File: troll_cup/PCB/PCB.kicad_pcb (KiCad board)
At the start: 2 copper layers, 45 x 45 mm, 13 parts, among them SW1 LEFT_BTN, SW2 RT_BTN, U1 ATtiny85-20P, U2 DFR0299

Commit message: New footprint
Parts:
- C1: footprint Capacitor_SMD:C_0603_1608Metric_Pad1.08x0.95mm_HandSolder -> Capacitor_THT:C_Disc_D5.0mm_W2.5mm_P2.50mm; moved to B.Cu
- R1: footprint Resistor_SMD:R_0805_2012Metric_Pad1.20x1.40mm_HandSolder -> Resistor_THT:R_Axial_DIN0204_L3.6mm_D1.6mm_P5.08mm_Horizontal; moved to B.Cu
- R2: footprint Resistor_SMD:R_0805_2012Metric_Pad1.20x1.40mm_HandSolder -> Resistor_THT:R_Axial_DIN0207_L6.3mm_D2.5mm_P7.62mm_Horizontal; moved to B.Cu
- SW1, SW2: footprint Library:Keypad -> Library:Keypad 2
- moved SW1 10.0 mm to (50.0, 68.5), turned to -90 degrees
- moved R2 5.90 mm to (77.0, 77.8)
- moved R1 4.65 mm to (62.0, 76.5)
- moved C1 2.61 mm to (58.0, 62.2)
- moved U1 1.41 mm to (65.2, 70.2)
- moved BAT1 1.00 mm to (66.0, 82.5)
- moved SPK1 1.00 mm to (77.0, 82.5)
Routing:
- net /VDD: track 130.8 -> 0.00 mm
- net /GND: track 47.7 -> 0.00 mm
- net Net-(U1-PB1): track 30.9 -> 0.00 mm
- net Net-(U1-XTAL2/PB4): track 28.1 -> 0.00 mm
- net Net-(SPK1-Pin_1): track 24.7 -> 0.00 mm
- net Net-(U2-TX): track 19.4 -> 0.00 mm
- net Net-(SPK1-Pin_2): track 18.9 -> 0.00 mm
- net Net-(U1-XTAL1/PB3): track 17.9 -> 0.00 mm
- net Net-(U1-AREF/PB0): track 7.55 -> 0.00 mm
- net Net-(U1-~{RESET}/PB5): track 3.27 -> 0.00 mm

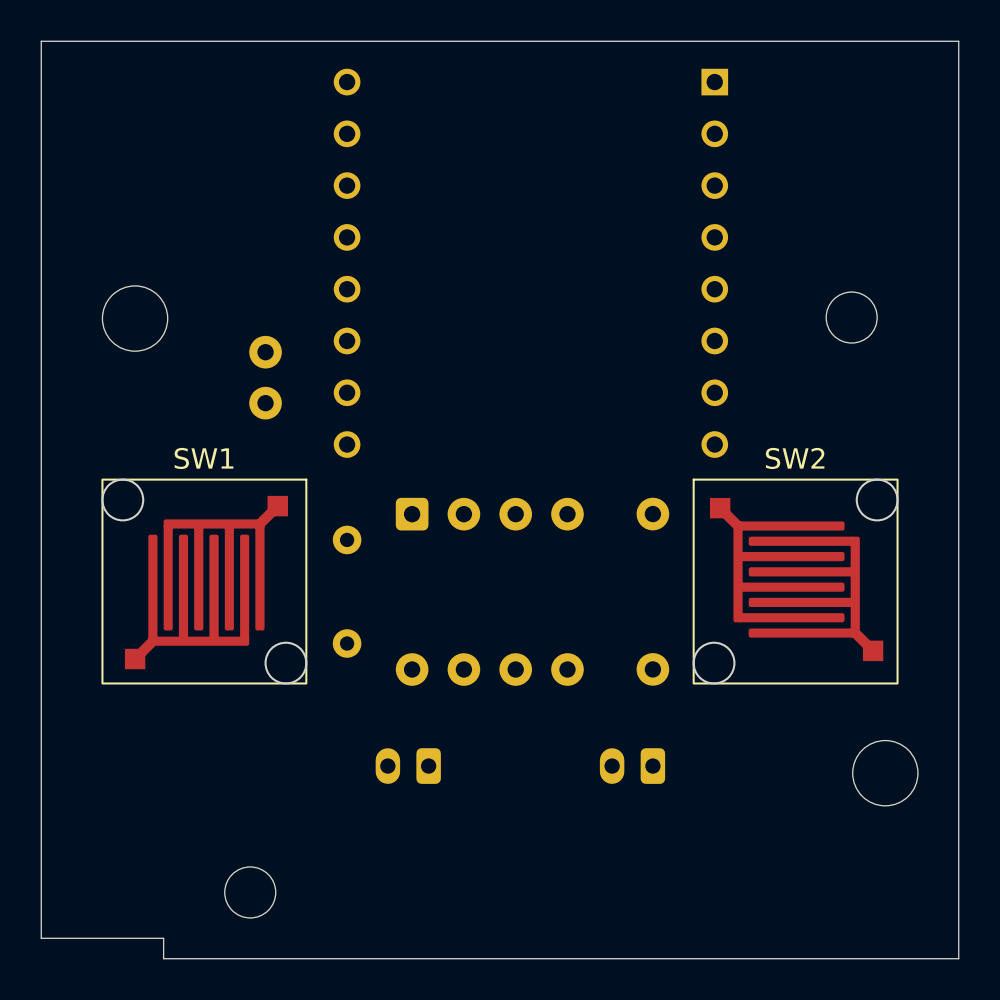
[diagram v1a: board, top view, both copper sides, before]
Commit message: Added traces
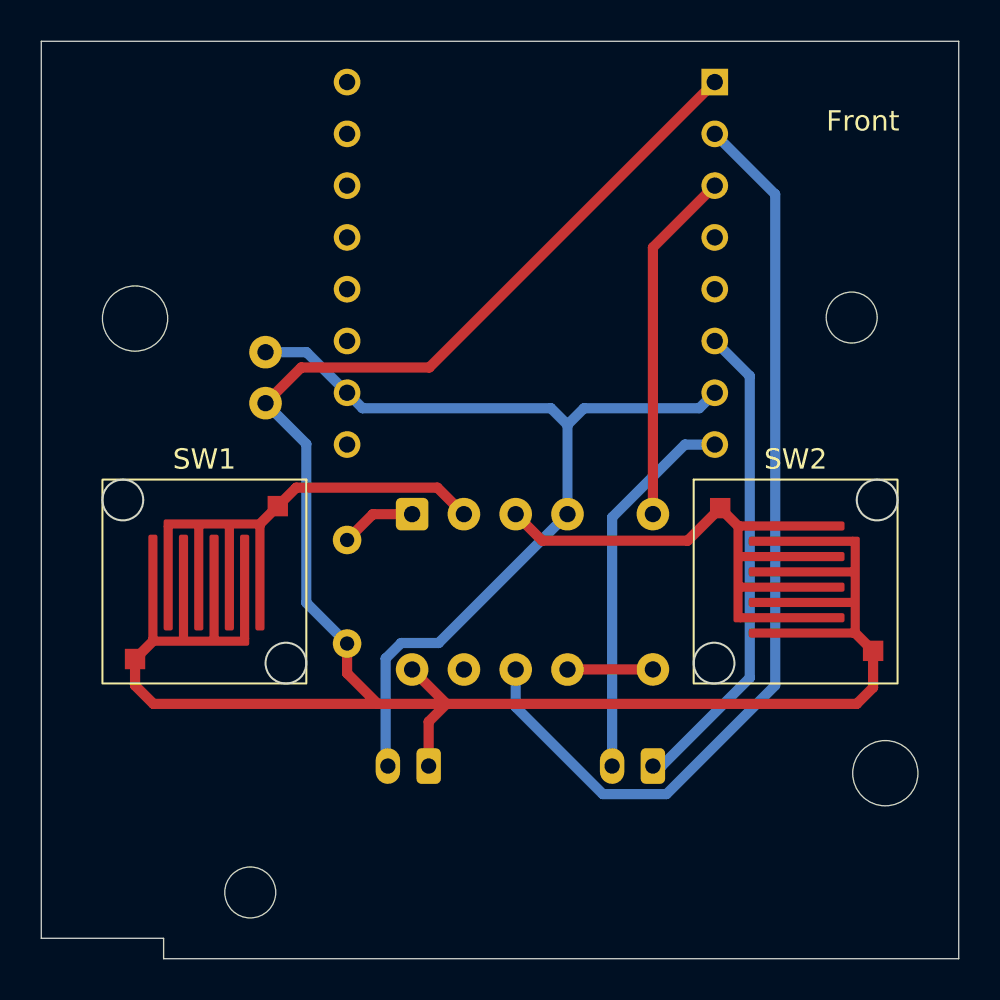
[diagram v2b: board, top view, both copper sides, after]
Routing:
- net /VDD: track 0.00 -> 91.4 mm
- net Net-(U1-PB1): track 0.00 -> 46.8 mm
- net /GND: track 0.00 -> 45.7 mm
- net Net-(SPK1-Pin_1): track 0.00 -> 23.8 mm
- net Net-(SPK1-Pin_2): track 0.00 -> 18.7 mm
- net Net-(U2-TX): track 0.00 -> 17.4 mm
- net Net-(U1-XTAL2/PB4): track 0.00 -> 11.2 mm
- net Net-(U1-XTAL1/PB3): track 0.00 -> 10.0 mm
- net Net-(U1-AREF/PB0): track 0.00 -> 4.19 mm
- net Net-(U1-~{RESET}/PB5): track 0.00 -> 3.71 mm
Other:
- board text added: "A SURPRISE FROM UNCLE TROLL STEVE"
- board text added: "Back"
- board text added: "Front"
- board text added: "I LOVE COFFEE IN MY COFFEE HOLE!"
